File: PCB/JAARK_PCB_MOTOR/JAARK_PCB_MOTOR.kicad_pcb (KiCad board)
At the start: 2 copper layers, 100 x 90 mm, 44 parts, among them IC1 TPS564242DRLR, IC10 DRV8231DDAR, IC9 DRV8231DDAR, J1 Battery Terminal, J2 Morpho_x2_SSW-119-01-T-D, J3 HC-05, J4 Metal Detector, J7 Metal Detector, M3_1 M3_1, M3_2 M3_2, M3_3 M3_3, M3_4 M3_4, Q1 SSM3J334RLF, Q3 BC237B, U1 3568

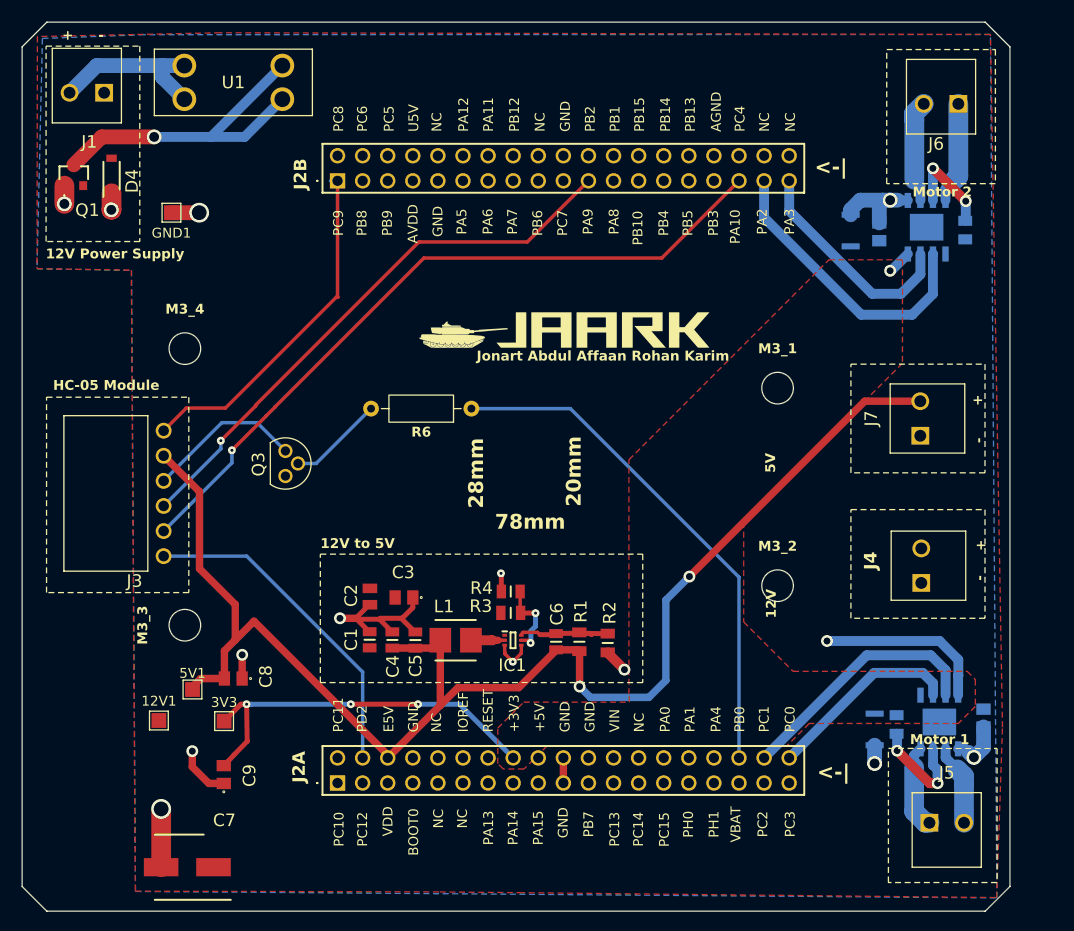
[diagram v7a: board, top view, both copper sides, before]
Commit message: Ultrasonic sensor code working on the STM32 with custom LCD driver
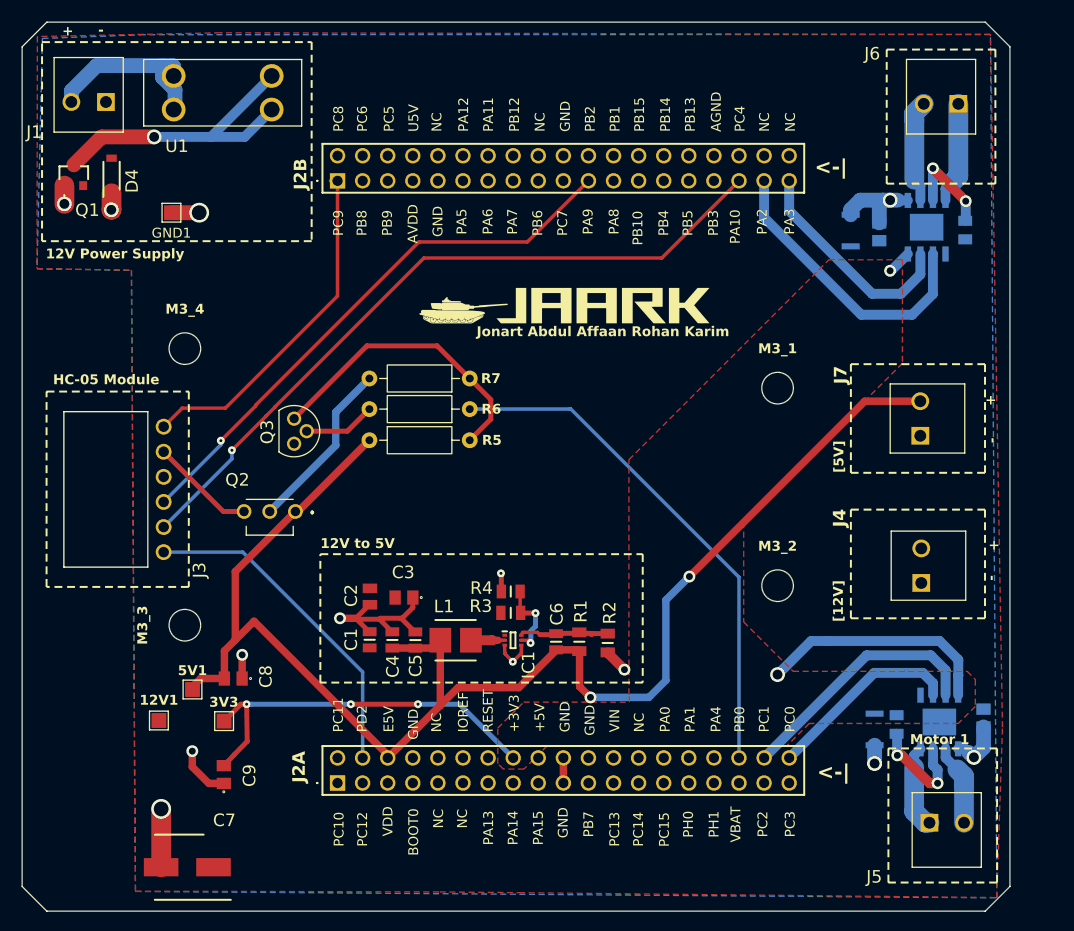
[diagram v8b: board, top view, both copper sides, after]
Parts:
- added Q2: 2N4403TFR, JAARK_lib:BC33740TA, F.Cu at (116.5, 95.1)
- added R5: 4.3kR, Resistor_THT:R_Axial_DIN0207_L6.3mm_D2.5mm_P10.16mm_Horizontal, F.Cu at (125.7, 87.3)
- added R7: 4.3kR, Resistor_THT:R_Axial_DIN0207_L6.3mm_D2.5mm_P10.16mm_Horizontal, F.Cu at (135.8, 81.0)
- moved Q3 3.39 mm to (118.1, 85.1)
- moved G*** 2.47 mm to (145.4, 73.5)
- moved U1 1.50 mm to (105.9, 53.8)
- moved J1 0.95 mm to (99.0, 53.0)
- moved J3 0.41 mm to (104.9, 98.6)
- moved R6 0.17 mm to (135.8, 84.1)
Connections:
- J3 pad 4: Net-(J3-GND) -> GND
- J3 pad 5: +5V -> Net-(J3-VCC)
- Q3 pad 1: Net-(J3-GND) -> Net-(Q3-C)
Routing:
- net Net-(Q3-C): track 0.00 -> 30.2 mm
- net Net-(Q2-B): track 0.00 -> 17.6 mm
- net Net-(J3-GND): track 16.0 -> 0.00 mm
- net Net-(J3-VCC): track 0.00 -> 10.6 mm
- net +3V3: track 59.6 -> 66.0 mm
- net +5V: track 143.7 -> 148.0 mm
- net Net-(Q1-D): track 34.1 -> 31.1 mm
- net Net-(Q3-B): track 9.94 -> 7.28 mm
- net Net-(J1-Pad2): track 17.1 -> 18.5 mm
- net /ST_HC: track 33.7 -> 34.4 mm
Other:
- board text added: "60mm"
- board text added: "[12V]"
- board text added: "[5V]"
- board text removed: "12V"
- board text removed: "5V"
- board text removed: "78mm"
